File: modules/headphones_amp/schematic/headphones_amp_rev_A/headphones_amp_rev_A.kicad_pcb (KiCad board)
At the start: 2 copper layers, 100 parts, among them J1 AudioJack3_SwitchTR, J2 AudioJack3_SwitchTR, Q1 BC140, Q10 BC548, Q11 BC548, Q12 BC140, Q13 BC160, Q14 BC548, Q15 BC557, Q16 BC548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

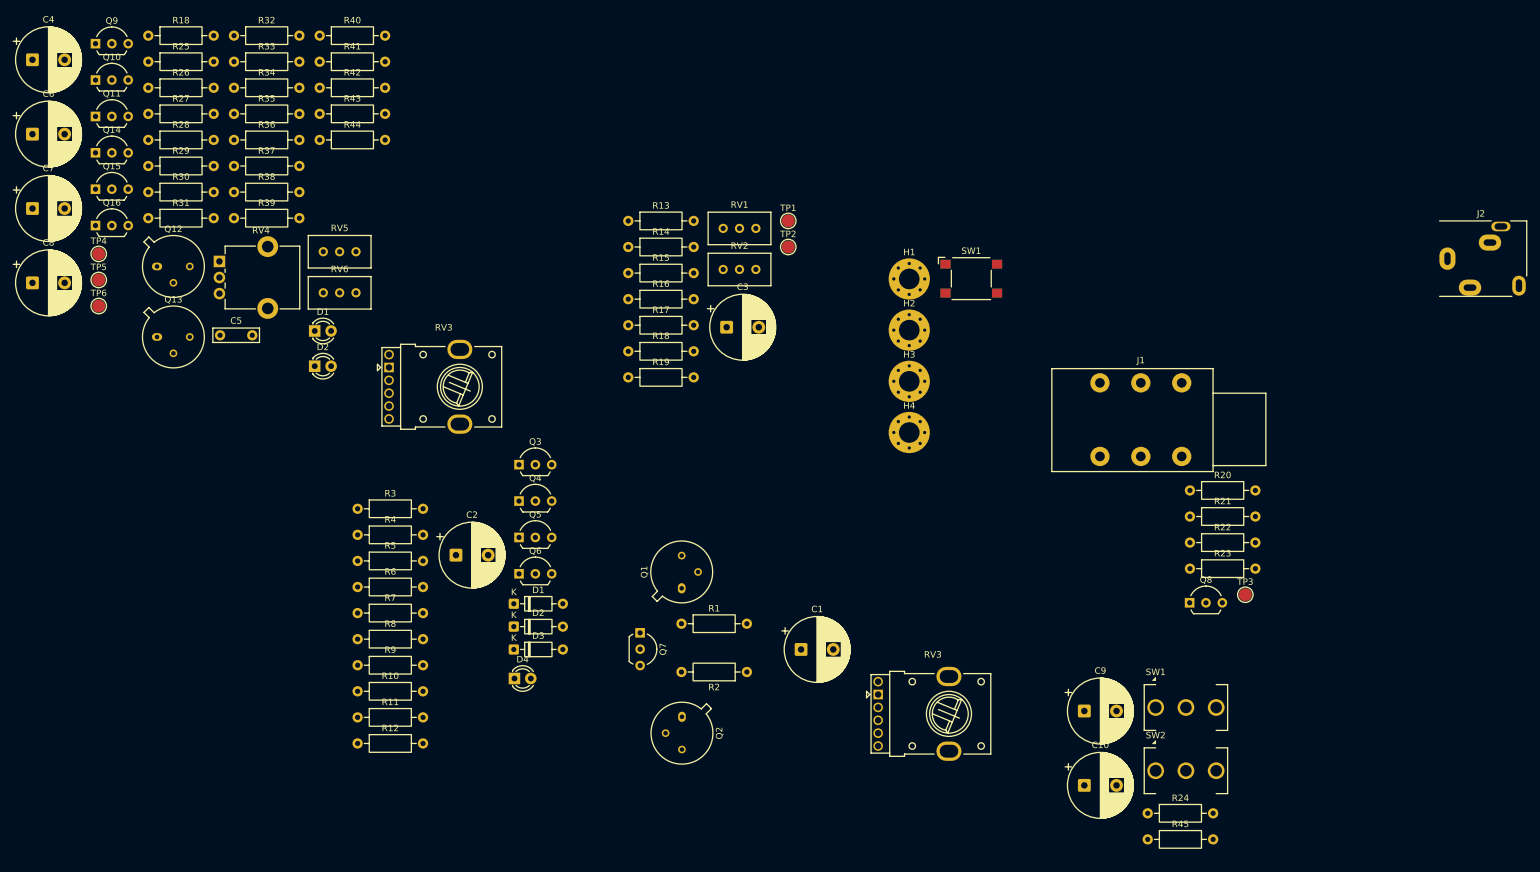
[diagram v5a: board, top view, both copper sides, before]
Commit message: attempt to fix wrong footprint
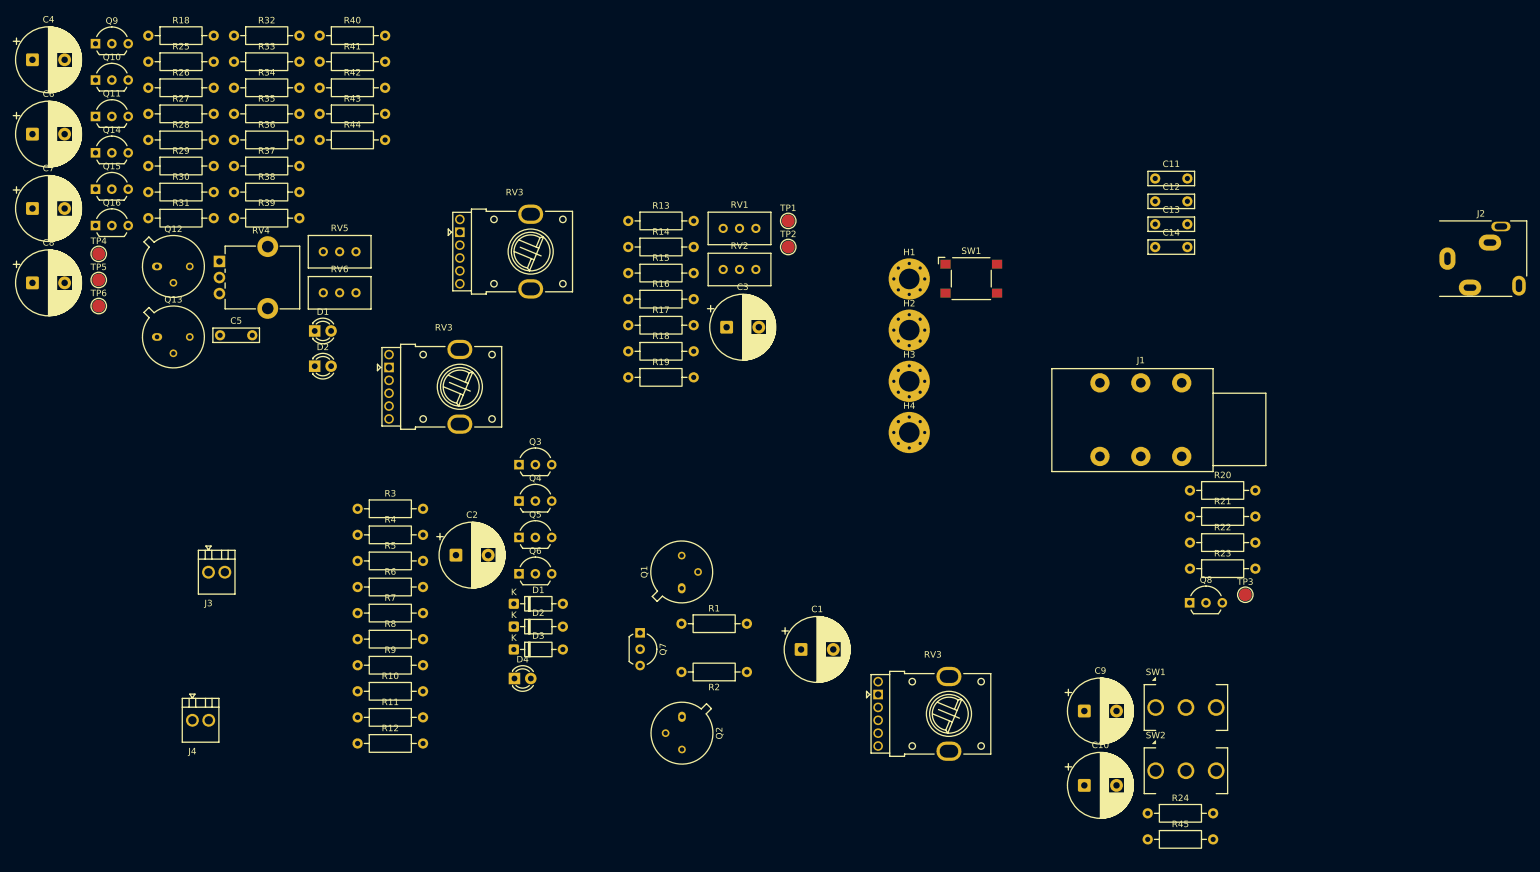
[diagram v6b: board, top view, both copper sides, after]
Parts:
- added C11: 100pF, Capacitor_THT:C_Rect_L7.0mm_W2.0mm_P5.00mm, F.Cu at (192.0, 40.9)
- added C12: 100pF, Capacitor_THT:C_Rect_L7.0mm_W2.0mm_P5.00mm, F.Cu at (192.0, 44.4)
- added C13: 100pF, Capacitor_THT:C_Rect_L7.0mm_W2.0mm_P5.00mm, F.Cu at (192.0, 48.0)
- added C14: 100pF, Capacitor_THT:C_Rect_L7.0mm_W2.0mm_P5.00mm, F.Cu at (192.0, 51.5)
- added J3: Conn_01x02, ProjectLib_Transient:WuerthElectronik_WR_TBL_Series_2109_1x02_P2.54mm_Horizontal, F.Cu at (45.0, 102.0)
- added J4: Conn_01x02, ProjectLib_Transient:WuerthElectronik_WR_TBL_Series_2109_1x02_P2.54mm_Horizontal, F.Cu at (42.5, 125.0)
- added RV3: R_Potentiometer_Dual_Shield_US, ProjectLib_Transient:Potentiometer_Bourns_PTV112-4_Dual_Vertical, F.Cu at (84.0, 49.2)
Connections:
- C10 pad 1: unconnected-(C10-Pad1) -> Net-(C10-Pad1)
- C10 pad 2: unconnected-(C10-Pad2) -> Net-(Q9-B)
- Q9 pad 2: unconnected-(Q9-B-Pad2) -> Net-(Q9-B)
- R21 pad 2: Net-(R21-Pad2) -> unconnected-(R21-Pad2)
- R24 pad 1: unconnected-(R24-Pad1) -> +12V
- R24 pad 2: Net-(R24-Pad2) -> Net-(Q9-B)
- R45 pad 1: Net-(R24-Pad2) -> Net-(Q9-B)
- RV3 pad 1: unconnected-(RV3-Pad1) -> Net-(J3-Pin_2)
- RV3 pad 6: unconnected-(RV3B-3-Pad6) -> Net-(J4-Pin_2)
- SW1 pad 2: unconnected-(SW1-Pad2) -> +12V
- SW2 pad 2: unconnected-(SW2-Pad2) -> Net-(C10-Pad1)
- SW2 pad 3: Net-(RV3B-2) -> Net-(RV3-Pad5)

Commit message: fixed the footprint issue with the PTV
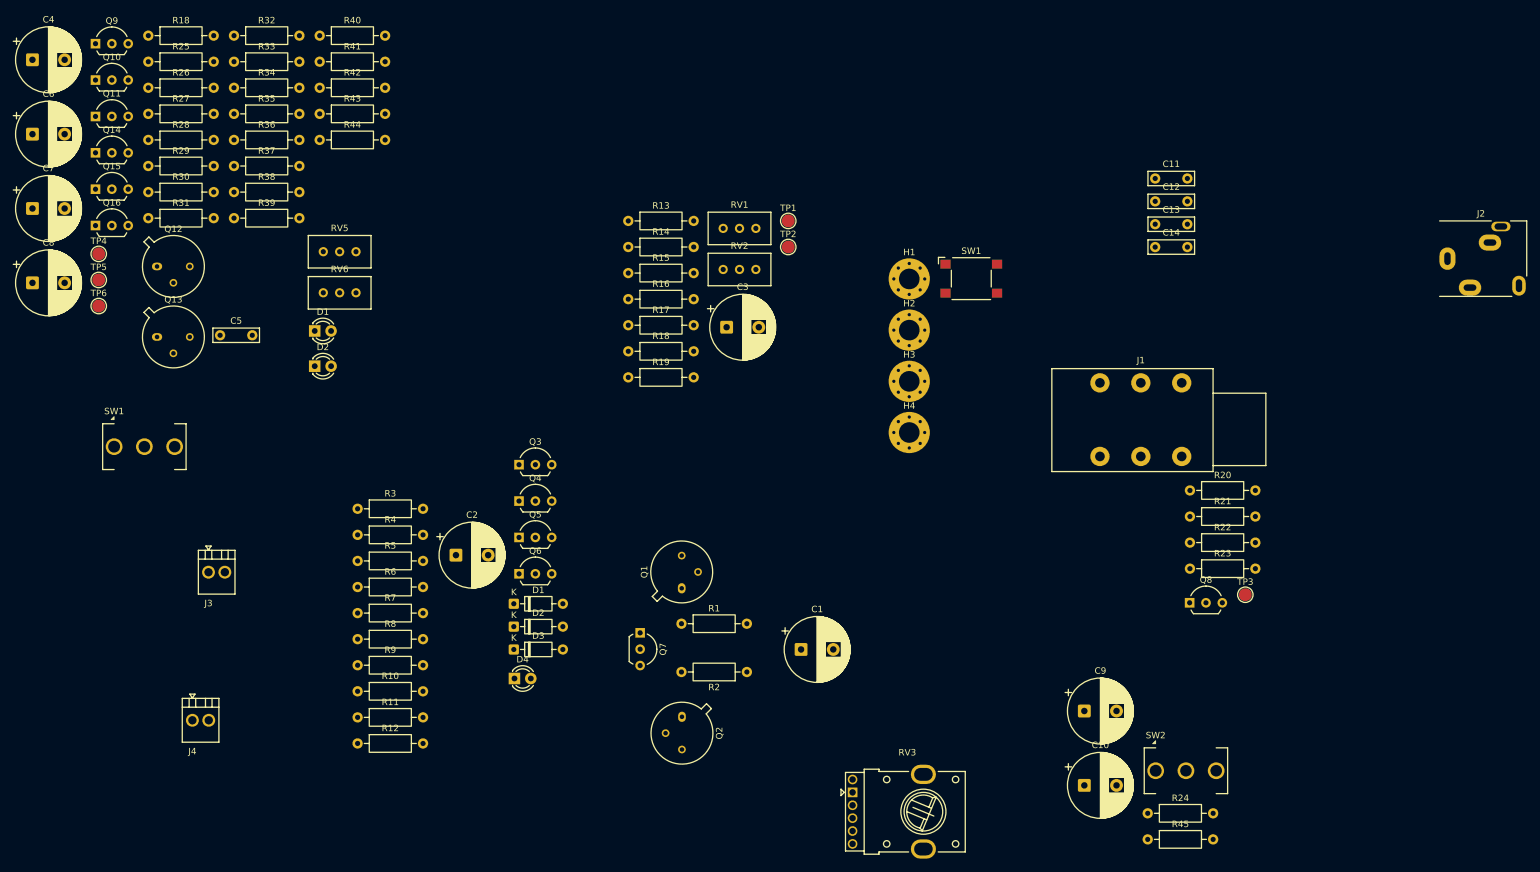
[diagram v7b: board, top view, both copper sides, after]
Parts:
- removed the RV3 at (73.0, 70.2)
- removed the RV3 at (149.0, 121.0)
- removed the RV3 at (84.0, 49.2)
- removed RV4: 1k, Potentiometer_THT:Potentiometer_Alpha_RD901F-40-00D_Single_Vertical_CircularHoles
- added RV3: R_Potentiometer_Dual_Shield_US, ProjectLib_Transient:Potentiometer_Bourns_PTV112-4_Dual_Vertical, F.Cu at (145.0, 136.2)
- moved SW1 166.8 mm to (30.3, 82.5)

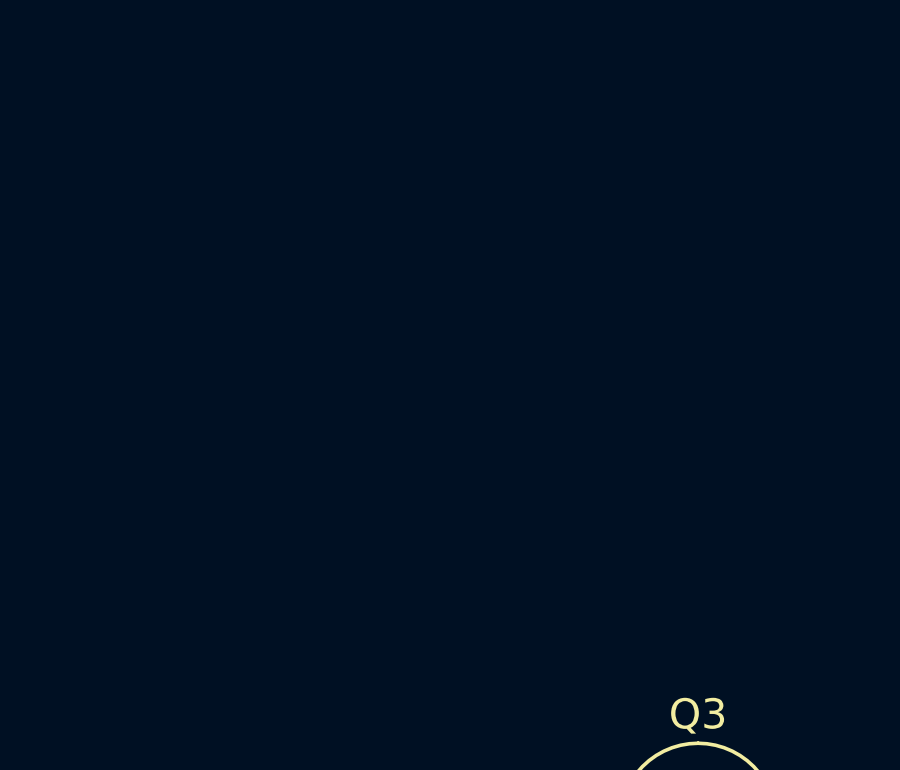
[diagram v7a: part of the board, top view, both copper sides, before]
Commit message: added datasheets
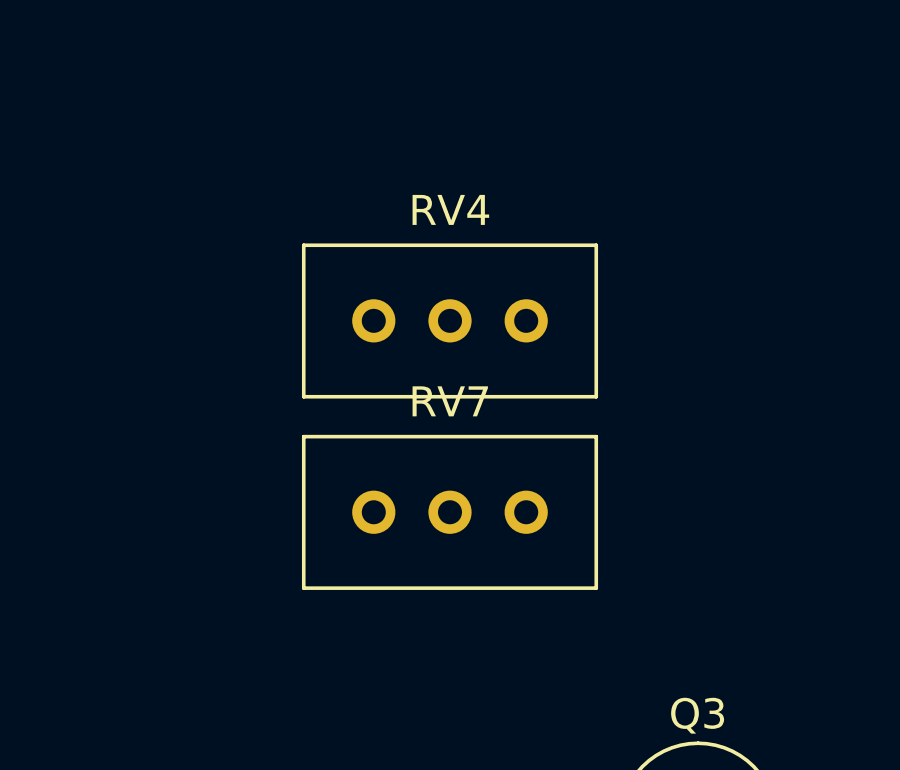
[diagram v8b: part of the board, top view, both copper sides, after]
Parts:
- added RV4: 50, Potentiometer_THT:Potentiometer_Bourns_3296W_Vertical, F.Cu at (90.0, 68.6)
- added RV7: 50, Potentiometer_THT:Potentiometer_Bourns_3296W_Vertical, F.Cu at (90.0, 75.0)
- RV3: value R_Potentiometer_Dual_Shield_US -> 68k
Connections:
- R37 pad 1: Net-(Q13-C) -> Net-(R37-Pad1)
- R6 pad 1: Net-(Q2-C) -> Net-(R6-Pad1)
